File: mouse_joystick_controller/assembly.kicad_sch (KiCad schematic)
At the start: 8 parts

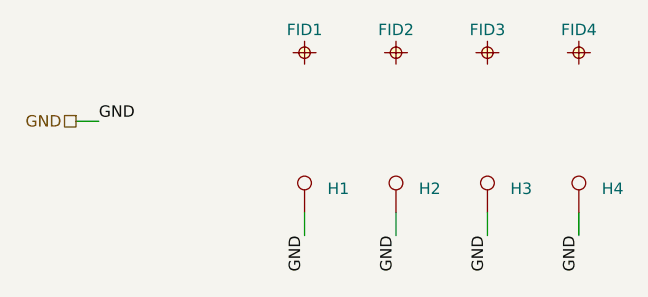
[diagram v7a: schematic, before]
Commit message: Test pin rcpt
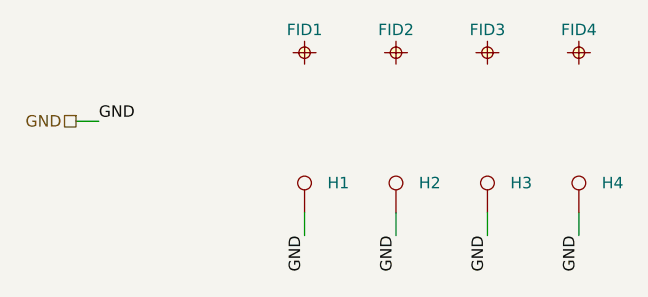
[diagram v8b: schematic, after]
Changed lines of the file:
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@@
   (title_block
     (title "mouse_joystick_controller")
-    (date "2023-06-07")
+    (date "2023-06-09")
     (rev "2.0")
     (company "Howard Hughes Medical Institute")
@@
       (effects (font (size 1.27 1.27)) hide)
     )
+    (property "Sim.Enable" "0" (at 147.32 88.9 0)
+      (effects (font (size 1.27 1.27)) hide)
+    )
     (instances
       (project "mouse_joystick_controller"
@@
       (effects (font (size 1.27 1.27)) hide)
     )
+    (property "Sim.Enable" "0" (at 167.64 88.9 0)
+      (effects (font (size 1.27 1.27)) hide)
+    )
     (instances
       (project "mouse_joystick_controller"
@@
       (effects (font (size 1.27 1.27)) hide)
     )
+    (property "Sim.Enable" "0" (at 157.48 88.9 0)
+      (effects (font (size 1.27 1.27)) hide)
+    )
     (instances
       (project "mouse_joystick_controller"
@@
   (symbol (lib_id "Janelia:MOUNTING_HOLE_3") (at 147.32 106.68 0) (unit 1)
     (in_bom no) (on_board yes) (dnp no) (fields_autoplaced)
-    (property "Reference" "H2" (at 149.86 104.013 0)
+    (property "Reference" "H2" (at 149.86 103.378 0)
       (effects (font (size 1.27 1.27)) (justify left))
     )
@@
   (symbol (lib_id "Janelia:MOUNTING_HOLE_3") (at 167.64 106.68 0) (unit 1)
     (in_bom no) (on_board yes) (dnp no) (fields_autoplaced)
-    (property "Reference" "H4" (at 170.18 104.013 0)
+    (property "Reference" "H4" (at 170.18 103.378 0)
       (effects (font (size 1.27 1.27)) (justify left))
     )
@@
       (effects (font (size 1.27 1.27)) hide)
     )
+    (property "Sim.Enable" "0" (at 137.16 88.9 0)
+      (effects (font (size 1.27 1.27)) hide)
+    )
     (instances
       (project "mouse_joystick_controller"
@@
   (symbol (lib_id "Janelia:MOUNTING_HOLE_3") (at 137.16 106.68 0) (unit 1)
     (in_bom no) (on_board yes) (dnp no) (fields_autoplaced)
-    (property "Reference" "H1" (at 139.7 104.013 0)
+    (property "Reference" "H1" (at 139.7 103.378 0)
       (effects (font (size 1.27 1.27)) (justify left))
     )
@@
   (symbol (lib_id "Janelia:MOUNTING_HOLE_3") (at 157.48 106.68 0) (unit 1)
     (in_bom no) (on_board yes) (dnp no) (fields_autoplaced)
-    (property "Reference" "H3" (at 160.02 104.013 0)
-      (effects (font (size 1.27 1.27)) (justify left))
-    )
+    (property "Reference" "H3" (at 160.02 103.378 0)
+      (effects (font (size 1.27 1.27)) (justify left))
+    )
